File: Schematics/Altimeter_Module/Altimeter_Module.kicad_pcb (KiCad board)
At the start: 2 copper layers, 4 parts, among them U1 KX134-1211, U2 MS560702BA03-50, U6 STM32F103CBTx, Y1 16MHz

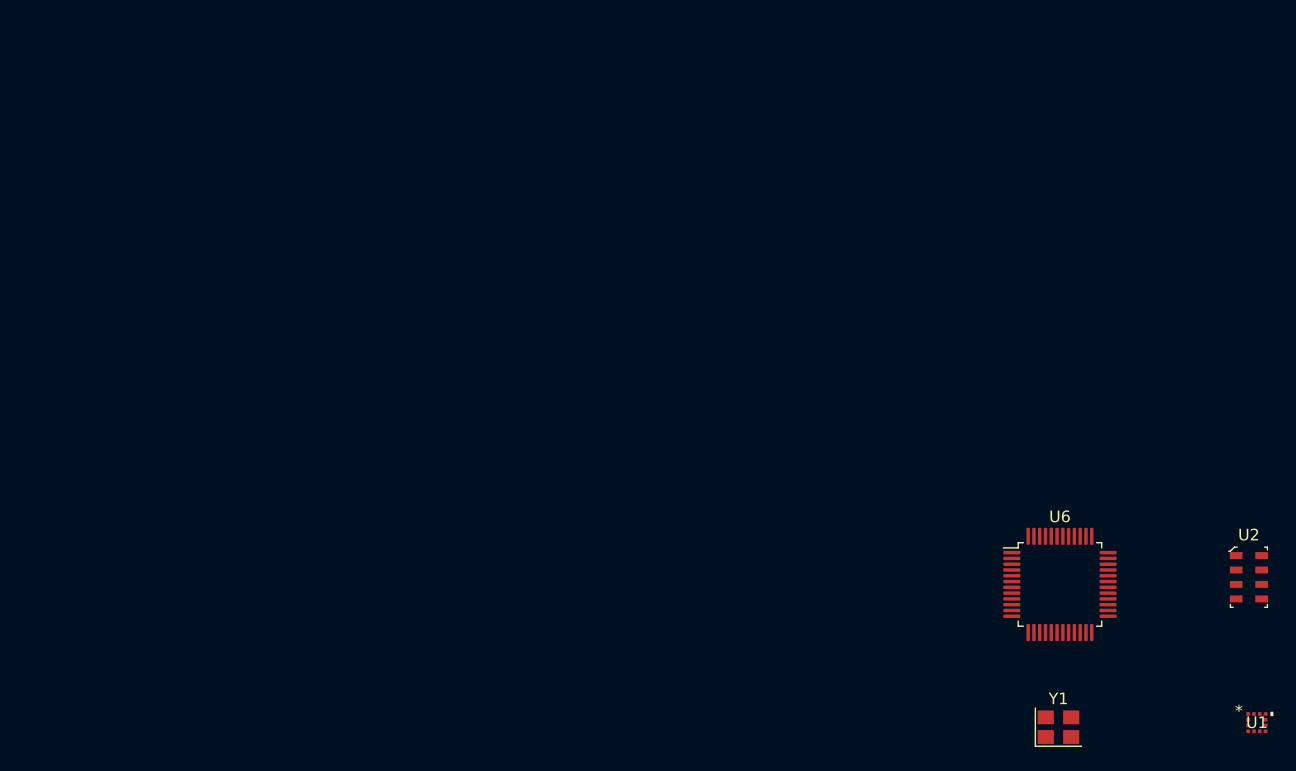
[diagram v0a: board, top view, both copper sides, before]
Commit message: Fixed footprints and added PCB template
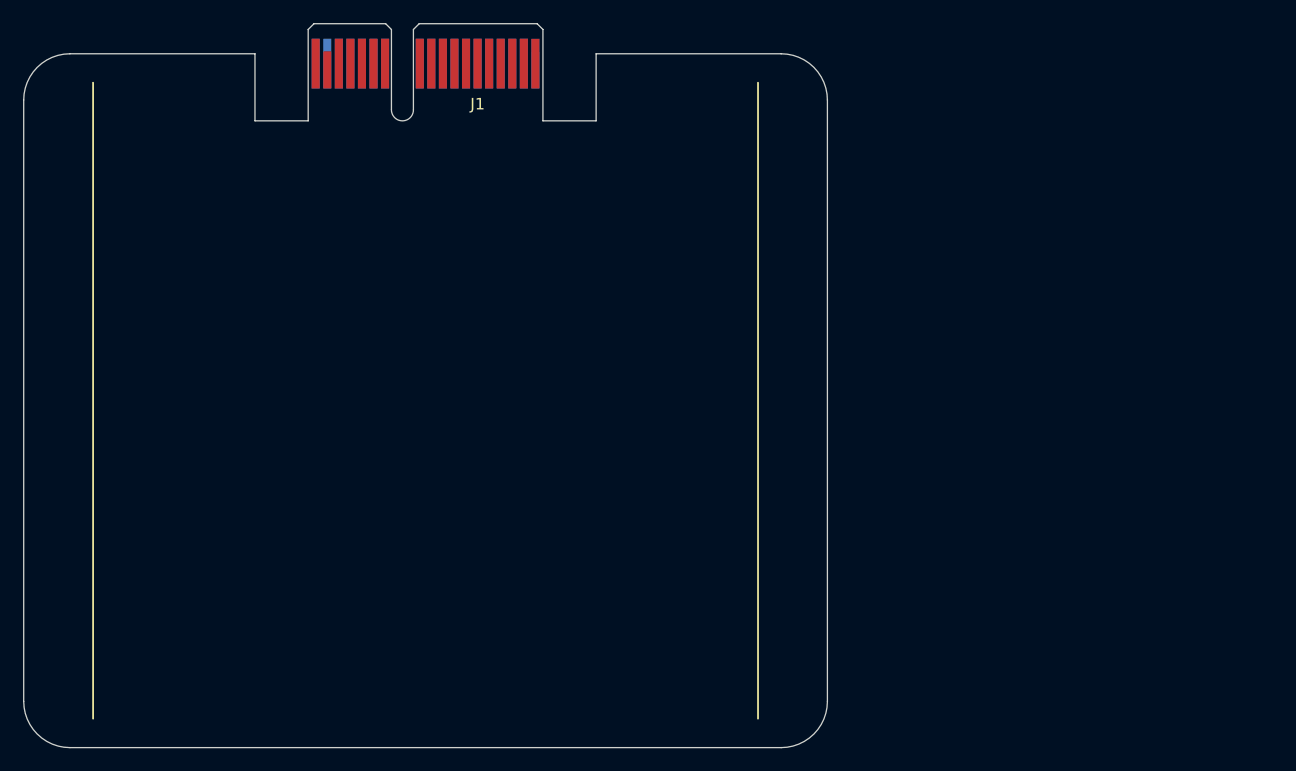
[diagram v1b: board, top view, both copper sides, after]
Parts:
- removed U1: KX134-1211, kx133:LGA12_2X2X0P9_ROM
- removed U2: MS560702BA03-50, digikey-footprints:SMD-8_5x3mm
- removed U6: STM32F103CBTx, Package_QFP:LQFP-48_7x7mm_P0.5mm
- removed Y1: 16MHz, Crystal:Crystal_SMD_3225-4Pin_3.2x2.5mm
- added J1: Stack Male Edge Connector, Connector_PCBEdge:BUS_PCIexpress_x1, F.Cu at (66.4, 21.0)
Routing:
- added copper zone on In1.Cu, net GND
- added copper zone on In2.Cu, net GND
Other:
- board outline added: 69.5 x 60 mm
- copper layers 2 -> 4
- board text added: "PLACE ACCEL EXACTLY HERE (NON-NEGOTIABLE)"
- board text added: "PLACE USB, SWD, E-MATCH CONNECTORS HERE (okay if e-match on bottom)"
- board text added: "USE GRID THAT IS SOME MULTIPLE OF 0.1mm (0.1mm, 0.2mm, 0.5mm, 1.0mm, etc)"
- board text added: "check communications module for examples"

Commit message: progress 9:42 3/13
placing components
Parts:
- added BZ2: PKM13EPYH4000, footprints:Buzzer_12.6x9.5RM5.0, F.Cu at (69.0, 36.6)
- added C1: 100nF, Capacitor_SMD:C_0603_1608Metric, F.Cu at (54.8, 46.1)
- added C10: 10p, Capacitor_SMD:C_0603_1608Metric, F.Cu at (48.5, 61.2)
- added C11: 10uF, Capacitor_SMD:CP_Elec_4x5.4, F.Cu at (48.5, 99.1)
- added C12: 100n, Capacitor_SMD:C_0402_1005Metric, F.Cu at (50.6, 55.0)
- added C13: 100n, Capacitor_SMD:C_0402_1005Metric, F.Cu at (54.0, 51.9)
- added C14: 100uF, Capacitor_SMD:CP_Elec_6.3x5.9, F.Cu at (38.4, 46.2)
- added C15: 100n, Capacitor_SMD:C_0402_1005Metric, F.Cu at (62.2, 55.1)
- added C17: 100n, Capacitor_SMD:C_0402_1005Metric, F.Cu at (60.2, 62.5)
- added C18: 0.1uF, Capacitor_SMD:C_0603_1608Metric, F.Cu at (47.0, 50.6)
- added C19: 10n, Capacitor_SMD:C_0603_1608Metric, F.Cu at (50.2, 61.2)
- added C2: 1uF, Capacitor_SMD:C_0603_1608Metric, F.Cu at (68.6, 148.8)
- added C20: 1uF, Capacitor_SMD:C_0805_2012Metric, F.Cu at (49.1, 66.3)
- added C21: 1uF, Capacitor_SMD:C_0805_2012Metric, F.Cu at (49.1, 63.9)
- added C22: 0.1u, Capacitor_SMD:C_0603_1608Metric, F.Cu at (64.6, 35.5)
- added C23: 0.1u, Capacitor_SMD:C_0603_1608Metric, F.Cu at (49.3, 35.4)
- added C24: 100nF, Capacitor_SMD:C_0603_1608Metric, F.Cu at (64.6, 141.3)
- added C25: 2.2nF, Capacitor_SMD:C_0603_1608Metric, F.Cu at (64.6, 138.8)
- added C26: 10nF, Capacitor_SMD:C_0603_1608Metric, F.Cu at (61.2, 45.8)
- added C3: 100nF, Capacitor_SMD:C_0603_1608Metric, F.Cu at (38.6, 53.8)
- added C30: 100nF, Capacitor_SMD:C_0603_1608Metric, F.Cu at (64.6, 133.8)
- added C31: 10uF, Capacitor_SMD:C_0603_1608Metric, F.Cu at (32.4, 71.4)
- added C32: 10uF, Capacitor_SMD:C_0603_1608Metric, F.Cu at (43.0, 68.7)
- added C4: 1uF, Capacitor_SMD:C_0603_1608Metric, F.Cu at (68.6, 143.8)
- added C5: 100nF, Capacitor_SMD:C_0603_1608Metric, F.Cu at (59.0, 46.1)
- added C6: 1uF, Capacitor_SMD:C_0603_1608Metric, F.Cu at (68.6, 138.8)
- added C7: 10p, Capacitor_SMD:C_0603_1608Metric, F.Cu at (48.5, 58.0)
- added C8: 100nF, Capacitor_SMD:C_0603_1608Metric, F.Cu at (68.6, 133.8)
- added C9: 100nF, Capacitor_SMD:C_0603_1608Metric, F.Cu at (65.5, 43.5)
- added D1: PWR_LED (GRN), LED_SMD:LED_0805_2012Metric, F.Cu at (38.5, 130.3)
- added D2: WS2812B, LED_SMD:LED_WS2812B_PLCC4_5.0x5.0mm_P3.2mm, F.Cu at (35.1, 26.9)
- added D3: DB_LED (YLW), LED_SMD:LED_0603_1608Metric, F.Cu at (84.1, 116.5)
- added D4: WS2812B, LED_SMD:LED_WS2812B_PLCC4_5.0x5.0mm_P3.2mm, F.Cu at (35.1, 33.6)
- added D5: 1N5819WS, Diode_SMD:D_SOD-323, F.Cu at (54.5, 100.5)
- added D6: 1N5819WS, Diode_SMD:D_SOD-323, F.Cu at (54.5, 97.6)
- added D7: FIRE_MAIN (RED), LED_SMD:LED_0603_1608Metric, F.Cu at (84.1, 114.0)
- added D8: FIRE_DRGE (RED), LED_SMD:LED_0603_1608Metric, F.Cu at (84.1, 111.4)
- added FB1: 100R, Resistor_SMD:R_0805_2012Metric, F.Cu at (52.1, 65.1)
- added J2: Main E-Match, footprints:CONN_2-1445057-2_TYCO, F.Cu at (72.1, 78.2)
- added J3: Drogue E-Match, footprints:CONN_2-1445057-2_TYCO, F.Cu at (79.9, 129.0)
- added J4: USB_B_Micro, footprints:USB_Micro-B_Amphenol_10118194_Horizontal, F.Cu at (41.4, 77.4)
- added J5: SWD_01x04_Pin, SWD_Header:SWD_PinHeader_1x04_P2.54mm_Horizontal, F.Cu at (57.2, 69.7)
- added Q1: AO3400A, Package_TO_SOT_SMD:SOT-23, F.Cu at (71.1, 66.0)
- added Q2: AO4406AL, Package_SO:SOIC-8_3.9x4.9mm_P1.27mm, F.Cu at (78.4, 65.1)
- added Q3: AO3400A, Package_TO_SOT_SMD:SOT-23, F.Cu at (68.2, 106.9)
- added Q4: AO3400A, Package_TO_SOT_SMD:SOT-23, F.Cu at (68.2, 102.4)
- added Q5: AO4406AL, Package_SO:SOIC-8_3.9x4.9mm_P1.27mm, F.Cu at (44.0, 117.8)
- added R1: 4.7k, Resistor_SMD:R_0603_1608Metric, F.Cu at (59.3, 64.4)
- added R10: 30k, Resistor_SMD:R_0603_1608Metric, F.Cu at (60.6, 128.8)
- added R11: 10k, Resistor_SMD:R_0603_1608Metric, F.Cu at (56.6, 151.4)
- added R12: 100k, Resistor_SMD:R_0603_1608Metric, F.Cu at (56.6, 148.8)
- added R13: 100k, Resistor_SMD:R_0603_1608Metric, F.Cu at (56.6, 146.3)
- added R14: 510R, Resistor_SMD:R_0603_1608Metric, F.Cu at (56.6, 143.8)
- added R15: 10k, Resistor_SMD:R_0603_1608Metric, F.Cu at (56.6, 141.3)
- added R16: 1k, Resistor_SMD:R_0603_1608Metric, F.Cu at (79.9, 52.7)
- added R17: 100k, Resistor_SMD:R_0603_1608Metric, F.Cu at (56.6, 136.3)
- added R18: 510R, Resistor_SMD:R_0603_1608Metric, F.Cu at (56.6, 133.8)
- added R19: 10k, Resistor_SMD:R_0603_1608Metric, F.Cu at (56.6, 131.3)
- added R2: 10k, Resistor_SMD:R_0603_1608Metric, F.Cu at (60.6, 148.8)
- added R20: 510R, Resistor_SMD:R_0603_1608Metric, F.Cu at (56.6, 128.8)
- added R21: 100k, Resistor_SMD:R_0603_1608Metric, F.Cu at (52.6, 151.4)
- added R22: 100k, Resistor_SMD:R_0603_1608Metric, F.Cu at (52.6, 148.8)
- added R23: 100k, Resistor_SMD:R_0603_1608Metric, F.Cu at (52.6, 146.3)
- added R24: 510R, Resistor_SMD:R_0603_1608Metric, F.Cu at (52.6, 143.8)
- added R25: 10k, Resistor_SMD:R_0603_1608Metric, F.Cu at (52.6, 141.3)
- added R26: 510R, Resistor_SMD:R_0603_1608Metric, F.Cu at (52.6, 138.8)
- added R27: 510R, Resistor_SMD:R_0603_1608Metric, F.Cu at (52.6, 136.3)
- added R3: 4.7k, Resistor_SMD:R_0603_1608Metric, F.Cu at (56.2, 63.9)
- added R4: 10k, Resistor_SMD:R_0603_1608Metric, F.Cu at (60.6, 143.8)
- added R5: 820R, Resistor_SMD:R_0603_1608Metric, F.Cu at (60.6, 141.3)
- added R6: 10k, Resistor_SMD:R_0603_1608Metric, F.Cu at (60.6, 138.8)
- added R7: 560R, Resistor_SMD:R_0603_1608Metric, F.Cu at (60.6, 136.3)
- added R8: 1.5k, Resistor_SMD:R_0603_1608Metric, F.Cu at (60.6, 133.8)
- added R9: 510R, Resistor_SMD:R_0603_1608Metric, F.Cu at (60.6, 131.3)
- added SW1: SW_STM_RESET, Button_Switch_SMD:SW_Push_1P1T_XKB_TS-1187A, F.Cu at (61.5, 110.2)
- added SW2: SW_STM_BOOT_MODE, Button_Switch_SMD:SW_Push_1P1T_XKB_TS-1187A, F.Cu at (61.5, 103.6)
- added TP1: TP_BSENSE, TestPoint:TestPoint_Pad_1.5x1.5mm, F.Cu at (48.8, 150.8)
- added TP10: TP_SCL, TestPoint:TestPoint_Pad_1.5x1.5mm, F.Cu at (41.7, 147.3)
- added TP11: TP_CMAIN, TestPoint:TestPoint_Pad_1.5x1.5mm, F.Cu at (41.7, 143.7)
- added TP12: TP_CDRGE, TestPoint:TestPoint_Pad_1.5x1.5mm, F.Cu at (41.7, 140.2)
- added TP13: TP_PA5, TestPoint:TestPoint_Pad_1.5x1.5mm, F.Cu at (63.5, 57.7)
- added TP14: TP_PA6, TestPoint:TestPoint_Pad_1.5x1.5mm, F.Cu at (63.5, 61.1)
- added TP15: TP_PA7, TestPoint:TestPoint_Pad_1.5x1.5mm, F.Cu at (63.5, 64.2)
- added TP2: TP_ISENSE, TestPoint:TestPoint_Pad_1.5x1.5mm, F.Cu at (44.1, 47.8)
- added TP3: TP_GND, TestPoint:TestPoint_Pad_1.5x1.5mm, F.Cu at (48.8, 143.7)
- added TP4: TP_3V3, TestPoint:TestPoint_Pad_1.5x1.5mm, F.Cu at (48.8, 140.2)
- added TP5: TP_VSTACK, TestPoint:TestPoint_Pad_1.5x1.5mm, F.Cu at (45.2, 150.8)
- added TP6: TP_VUSB, TestPoint:TestPoint_Pad_1.5x1.5mm, F.Cu at (45.2, 147.3)
- added TP7: TP_VSWD, TestPoint:TestPoint_Pad_1.5x1.5mm, F.Cu at (45.2, 143.7)
- added TP8: TP_MUX, TestPoint:TestPoint_Pad_1.5x1.5mm, F.Cu at (45.2, 140.2)
- added TP9: TP_SDA, TestPoint:TestPoint_Pad_1.5x1.5mm, F.Cu at (41.7, 150.8)
- added U1: KX134-1211, Package_LGA:LGA-12_2x2mm_P0.5mm, F.Cu at (56.9, 46.0)
- added U10: ACS70331EOLC, footprints:SOIC127P600X175-8N, F.Cu at (49.3, 47.0)
- added U12: AMS1117-3.3, Package_TO_SOT_SMD:SOT-223-3_TabPin2, F.Cu at (37.7, 69.2)
- added U2: MS560702BA03-50, digikey-footprints:SMD-8_5x3mm, F.Cu at (35.6, 55.1)
- added U3: W25Q128JVS, Package_SO:SOIC-8_5.23x5.23mm_P1.27mm, F.Cu at (70.5, 58.1)
- added U4: LM66100DCKR, LMR66100:SC-70-6_Handsoldering, F.Cu at (81.1, 26.1)
- added U5: LM66100DCKR, LMR66100:SC-70-6_Handsoldering, F.Cu at (81.1, 57.7)
- added U6: STM32F103CBTx, Package_QFP:LQFP-48_7x7mm_P0.5mm, F.Cu at (56.5, 57.6)
- added U7: LM66100DCKR, LMR66100:SC-70-6_Handsoldering, F.Cu at (80.5, 46.6)
- added U8: ISO1042BDWVR, ISO1042:SOIC-8 ISO1042BDWV, F.Cu at (56.9, 32.5)
- added U9: MPU-6050, Sensor_Motion:InvenSense_QFN-24_4x4mm_P0.5mm, F.Cu at (64.8, 47.8)
- added Y1: X322516MMB4SI, Crystal:Crystal_SMD_3225-4Pin_3.2x2.5mm, F.Cu at (45.9, 58.9)
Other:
- board text removed: "PLACE ACCEL EXACTLY HERE (NON-NEGOTIABLE)"

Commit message: progress 10:26 3/13
more components placed
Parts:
- D4: moved to B.Cu
- moved TP5 126.5 mm to (78.0, 28.7)
- moved C2 120.3 mm to (81.1, 29.2), turned to 0 degrees
- moved C6 102.6 mm to (81.2, 37.0), turned to 0 degrees
- moved C4 100.3 mm to (81.1, 44.3), turned to 0 degrees
- moved TP7 76.4 mm to (61.1, 69.0)
- moved TP6 75.7 mm to (44.1, 71.6)
- moved U5 16.5 mm to (81.1, 41.2)
- moved U7 12.8 mm to (81.2, 33.8)
- turned D4 to 180 degrees

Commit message: progress 12:30 3/14
very very rough work
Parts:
- J2, J3: moved to B.Cu
- moved R2 110.5 mm to (63.5, 38.4), turned to 0 degrees
- moved R14 97.9 mm to (73.8, 47.5), turned to -90 degrees
- moved R24 97.2 mm to (34.6, 48.3), turned to 0 degrees
- moved R15 95.0 mm to (76.5, 48.5)
- moved C30 94.1 mm to (53.3, 40.4), turned to -90 degrees
- moved J3 93.0 mm to (32.5, 49.0), turned to 90 degrees
- moved R4 90.2 mm to (82.2, 56.3), turned to 90 degrees
- moved R26 89.1 mm to (41.4, 50.4), turned to 90 degrees
- moved R25 88.4 mm to (41.4, 53.6), turned to -90 degrees
- moved R27 83.1 mm to (43.3, 53.7), turned to -90 degrees
- moved C8 80.7 mm to (79.7, 53.9)
- moved R6 80.4 mm to (71.0, 59.1), turned to -90 degrees
- moved TP11 78.6 mm to (70.5, 70.6)
- moved R12 75.4 mm to (73.5, 75.4), turned to -90 degrees
- moved TP12 75.0 mm to (54.7, 66.3)
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
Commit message: progress 3:22 3/14
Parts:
- moved TP4 108.4 mm to (33.6, 32.9)
- moved TP3 100.3 mm to (80.1, 48.4)
- moved C24 97.9 mm to (63.9, 43.4), turned to 90 degrees
- moved R5 95.1 mm to (50.5, 46.8)
- moved R23 92.3 mm to (34.7, 55.8)
- moved TP8 91.6 mm to (45.8, 48.6)
- moved TP9 90.6 mm to (32.4, 60.7)
- moved C25 87.5 mm to (63.2, 51.3)
- moved R21 85.2 mm to (64.2, 67.0)
- moved TP10 84.1 mm to (32.4, 63.7)
- moved R22 82.8 mm to (59.3, 66.3), turned to 0 degrees
- moved D1 82.3 mm to (50.3, 48.9), turned to 0 degrees
- moved D3 78.7 mm to (57.9, 49.4)
- moved R18 75.9 mm to (80.1, 61.6)
- moved R11 75.1 mm to (68.0, 77.2), turned to 90 degrees
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
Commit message: progress 12:00 3/15
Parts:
- moved C23 1.82 mm to (47.3, 33.3), turned to -90 degrees
- moved C30 0.27 mm to (53.1, 39.1)
- moved SW1 0.27 mm to (57.9, 40.2)
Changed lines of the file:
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@@
   )
   (footprint "Capacitor_SMD:C_0603_1608Metric" (layer "F.Cu")
-    (at 53.1 39.4 -90)
+    (at 53.1 39.125 -90)
     (descr "Capacitor SMD 0603 (1608 Metric), square (rectangular) end terminal, IPC_7351 nominal, (Body size source: IPC-SM-782 page 76, https://www.pcb-3d.com/wordpress/wp-content/uploads/ipc-sm-782a_amendment_1_and_2.pdf), generated with kicad-footprint-generator")
     (tags "capacitor")
@@
   )
   (footprint "Button_Switch_SMD:SW_Push_1P1T_XKB_TS-1187A" (layer "F.Cu")
-    (at 57.9 40.5 180)
+    (at 57.9 40.225 180)
     (descr "SMD Tactile Switch, http://www.helloxkb.com/public/images/pdf/TS-1187A-X-X-X.pdf")
     (tags "SPST Tactile Switch")
@@
   )
   (footprint "Capacitor_SMD:C_0603_1608Metric" (layer "F.Cu")
-    (at 47.512 35.105 90)
+    (at 47.3 33.3 -90)
     (descr "Capacitor SMD 0603 (1608 Metric), square (rectangular) end terminal, IPC_7351 nominal, (Body size source: IPC-SM-782 page 76, https://www.pcb-3d.com/wordpress/wp-content/uploads/ipc-sm-782a_amendment_1_and_2.pdf), generated with kicad-footprint-generator")
     (tags "capacitor")
@@
     (fp_line (start 0.8 0.4) (end -0.8 0.4)
       (stroke (width 0.1) (type solid)) (layer "F.Fab"))
-    (pad "1" smd roundrect (at -0.775 0 90) (size 0.9 0.95) (layers "F.Cu" "F.Paste" "F.Mask") (roundrect_rratio 0.25)
+    (pad "1" smd roundrect (at -0.775 0 270) (size 0.9 0.95) (layers "F.Cu" "F.Paste" "F.Mask") (roundrect_rratio 0.25)
       (net 1 "GND") (pintype "passive"))
-    (pad "2" smd roundrect (at 0.775 0 90) (size 0.9 0.95) (layers "F.Cu" "F.Paste" "F.Mask") (roundrect_rratio 0.25)
+    (pad "2" smd roundrect (at 0.775 0 270) (size 0.9 0.95) (layers "F.Cu" "F.Paste" "F.Mask") (roundrect_rratio 0.25)
       (net 3 "+5V") (pintype "passive"))
     (model "${KICAD6_3DMODEL_DIR}/Capacitor_SMD.3dshapes/C_0603_1608Metric.wrl"

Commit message: progress 2:00 3/16
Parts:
- D7, D8, Q1, Q2, Q4, Q5, R17, R18, R19, R20, R21, R22, R23, R24, R25, R26, R27, R9, TP11, TP12: moved to B.Cu
- moved TP4 143.7 mm to (173.0, 67.6), turned to -90 degrees
- moved D2 138.2 mm to (167.8, 66.0), turned to 180 degrees
- moved D4 138.2 mm to (167.8, 66.0)
- moved TP2 138.1 mm to (173.5, 85.9)
- moved C31 137.3 mm to (163.3, 112.6), turned to 180 degrees
- moved U12 135.7 mm to (167.8, 108.1)
- moved C14 135.1 mm to (168.0, 80.7), turned to 180 degrees
- moved TP6 134.9 mm to (173.6, 107.9), turned to 90 degrees
- moved U10 129.0 mm to (168.2, 87.5), turned to 0 degrees
- moved R5 128.3 mm to (169.5, 94.7)
- moved D1 127.6 mm to (170.4, 92.1)
- moved C32 125.0 mm to (162.3, 106.0)
- moved C18 124.1 mm to (167.7, 72.2), turned to 90 degrees
- moved TP8 121.9 mm to (165.3, 72.3)
- moved C30 114.3 mm to (159.1, 81.9), turned to 0 degrees
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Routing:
- removed copper zone on In1.Cu, net GND
- removed copper zone on In2.Cu, net GND
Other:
- board text added: "Find way to place e-match parts"

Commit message: Updated MS5607 footprint + added many 3D models
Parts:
- U2: footprint digikey-footprints:SMD-8_5x3mm -> footprints:MS5607_Handsolder
- U6: value STM32F103CBTx -> STM32F103CBT6
- moved U2 1.02 mm to (123.6, 84.1), turned to 0 degrees
